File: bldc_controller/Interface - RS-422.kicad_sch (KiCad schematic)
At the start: 2 parts, among them U11 SN65HVD35DR

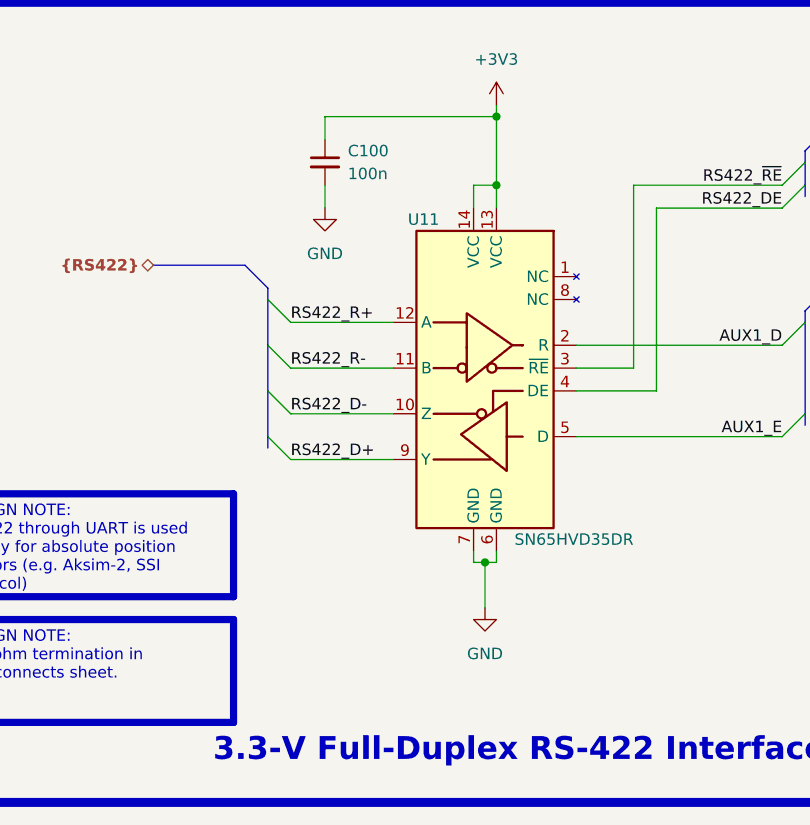
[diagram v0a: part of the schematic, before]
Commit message: schematic is complete. Replaced 5V buck and added pi filters.
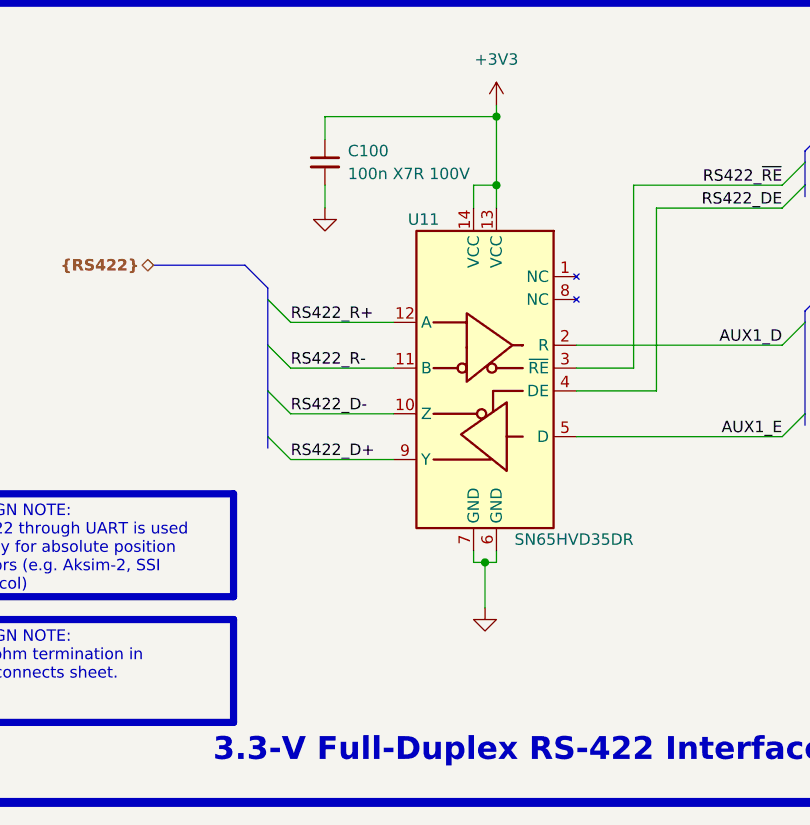
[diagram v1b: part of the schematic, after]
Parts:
- C100: value 100n -> 100n X7R 100V
- U11: footprint 0_interface_uart:SOIC-14 5.4mm -> 0_package_SO:SOIC-14 5.4mm
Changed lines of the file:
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@@
       (effects (font (size 1.27 1.27)) (justify left))
     )
-    (property "Value" "100n" (at 130.81 60.9663 0)
+    (property "Value" "100n X7R 100V" (at 130.81 60.9663 0)
       (effects (font (size 1.27 1.27)) (justify left))
     )
@@
     )
     (property "Value" "GND" (at 128.27 69.85 0)
-      (effects (font (size 1.27 1.27)))
+      (effects (font (size 1.27 1.27)) hide)
     )
     (property "Footprint" "" (at 128.27 64.77 0)
@@
     )
     (property "Value" "GND" (at 146.05 114.3 0)
-      (effects (font (size 1.27 1.27)))
+      (effects (font (size 1.27 1.27)) hide)
     )
     (property "Footprint" "" (at 146.05 109.22 0)
@@
       (effects (font (size 1.27 1.27)) (justify left))
     )
-    (property "Footprint" "0_interface_uart:SOIC-14 5.4mm" (at 146.05 107.95 0)
+    (property "Footprint" "0_package_SO:SOIC-14 5.4mm" (at 146.05 107.95 0)
       (effects (font (size 1.27 1.27)) hide)
     )

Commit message: added assembly files
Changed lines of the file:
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@@
   (symbol (lib_id "0_interface_uart:SN65HVD35DR") (at 146.05 85.09 0) (mirror y) (unit 1)
     (in_bom yes) (on_board yes) (dnp no)
-    (property "Reference" "U11" (at 140.97 66.04 0)
+    (property "Reference" "U11" (at 137.16 68.58 0)
       (effects (font (size 1.27 1.27)) (justify left))
     )
-    (property "Value" "SN65HVD35DR" (at 162.56 101.6 0)
+    (property "Value" "SN65HVD35DR" (at 137.16 71.12 0)
       (effects (font (size 1.27 1.27)) (justify left))
     )
